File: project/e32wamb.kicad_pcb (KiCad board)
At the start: 2 copper layers, 50 x 37 mm, 34 parts, among them J1 2059-302_998-403, J2 Conn_01x04, J3 Conn_01x03, Q1 AO3400, Q2 AO3400, Q3 AO3400, Q4 AO3400, Q5 AO3400, SW1 TS-1187A-B-A-B, U1 AP63203WU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

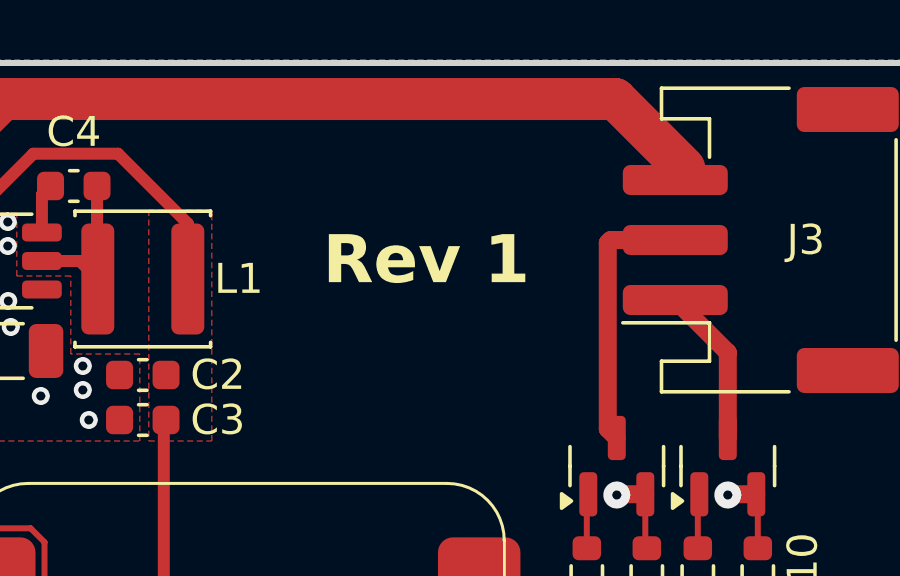
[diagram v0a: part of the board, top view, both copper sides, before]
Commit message: Add rotation offset for U1 (for jlcfab), bump revision
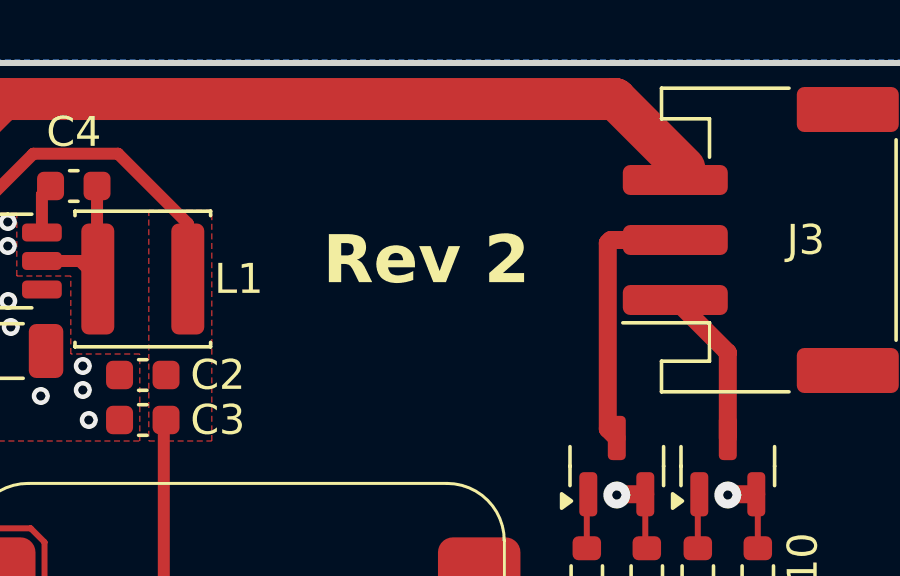
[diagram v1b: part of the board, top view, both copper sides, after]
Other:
- board text added: "Rev 2"
- board text removed: "Rev 1"
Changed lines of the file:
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@@
 	(title_block
 		(title "e32wamb pcb")
-		(date "2025-04-08")
-		(rev "1")
+		(date "2025-04-09")
+		(rev "2")
 		(company "wejn.org")
 		(comment 1 "Licensed under CC BY-SA 4.0")
@@
 			)
 		)
+		(property "FT Rotation Offset" "90"
+			(at 0 0 0)
+			(unlocked yes)
+			(layer "F.Fab")
+			(hide yes)
+			(effects
+				(font
+					(size 1 1)
+					(thickness 0.15)
+				)
+			)
+		)
 		(property ki_fp_filters "TSOT?23*")
 		(sheetname "/")
@@
 		)
 	)
-	(gr_text "Rev 1"
+	(gr_text "Rev 2"
 		(at 80.1 57.5 0)
 		(layer "F.SilkS")

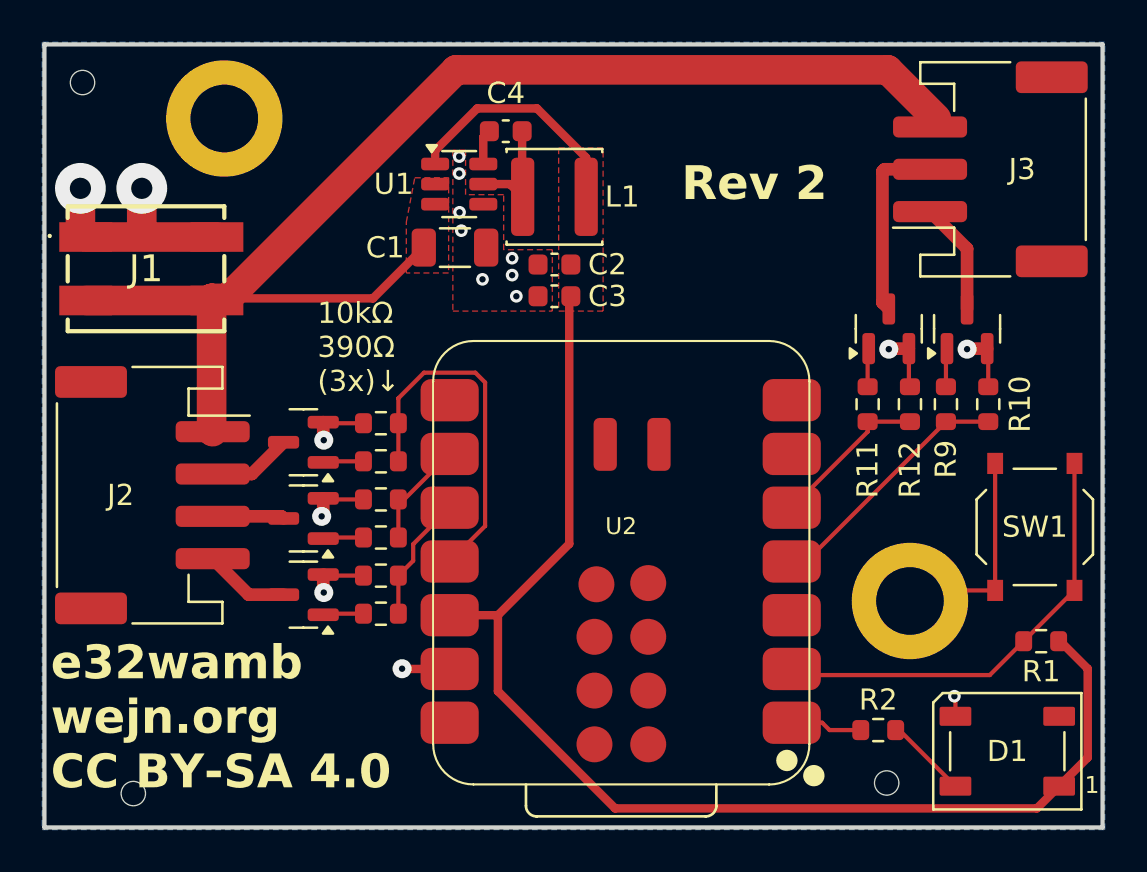
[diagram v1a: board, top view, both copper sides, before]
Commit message: Tune spacing between mounting holes; switch to vars for revision + date
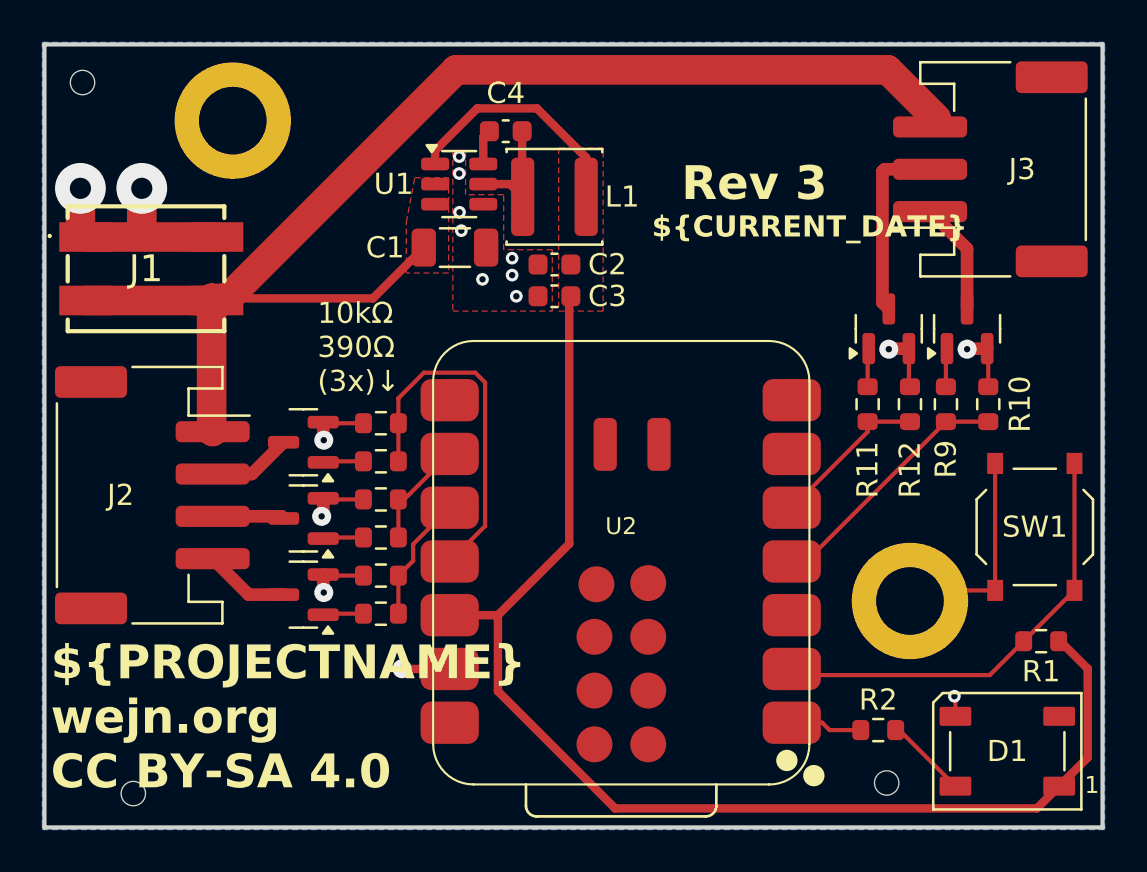
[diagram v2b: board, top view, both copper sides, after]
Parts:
- moved H1 0.41 mm to (58.9, 53.6)
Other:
- board text added: "${CURRENT_DATE}"
- board text added: "${PROJECTNAME} ${COMPANY} CC BY-SA 4.0"
- board text added: "Rev ${REVISION}"
- board text removed: "Rev 2"
- board text removed: "e32wamb wejn.org CC BY-SA 4.0"
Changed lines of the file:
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@@
 	(title_block
 		(title "e32wamb pcb")
-		(date "2025-04-09")
-		(rev "2")
+		(date "${CURRENT_DATE}")
+		(rev "3")
 		(company "wejn.org")
 		(comment 1 "Licensed under CC BY-SA 4.0")
@@
 	(footprint "MountingHole:MountingHole_3.2mm_M3_ISO14580_Pad"
 		(layer "F.Cu")
-		(at 58.5 53.5)
+		(at 58.9 53.6)
 		(descr "Mounting Hole 3.2mm, M3, ISO14580")
 		(tags "mounting hole 3.2mm m3 iso14580")
@@
 		(layer "Edge.Cuts")
 	)
+	(gr_text "${CURRENT_DATE}"
+		(at 78.7 59.2 0)
+		(layer "F.SilkS")
+		(effects
+			(font
+				(size 1 1)
+				(thickness 0.2)
+				(bold yes)
+			)
+			(justify left bottom)
+		)
+	)
 	(gr_text "10kΩ\n390Ω\n(3x)↓"
 		(at 62.9 66.5 0)
@@
 		)
 	)
-	(gr_text "e32wamb\nwejn.org\nCC BY-SA 4.0"
+	(gr_text "${PROJECTNAME}\n${COMPANY}\nCC BY-SA 4.0"
 		(at 50.3 85.3 0)
 		(layer "F.SilkS")
@@
 		)
 	)
-	(gr_text "Rev 2"
+	(gr_text "Rev ${REVISION}"
 		(at 80.1 57.5 0)
 		(layer "F.SilkS")

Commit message: Add keepout zone around the antenna
I thought I could do without because I'll be using an external antenna,
but it hardly costs anything. So why not have the keepout just in case.
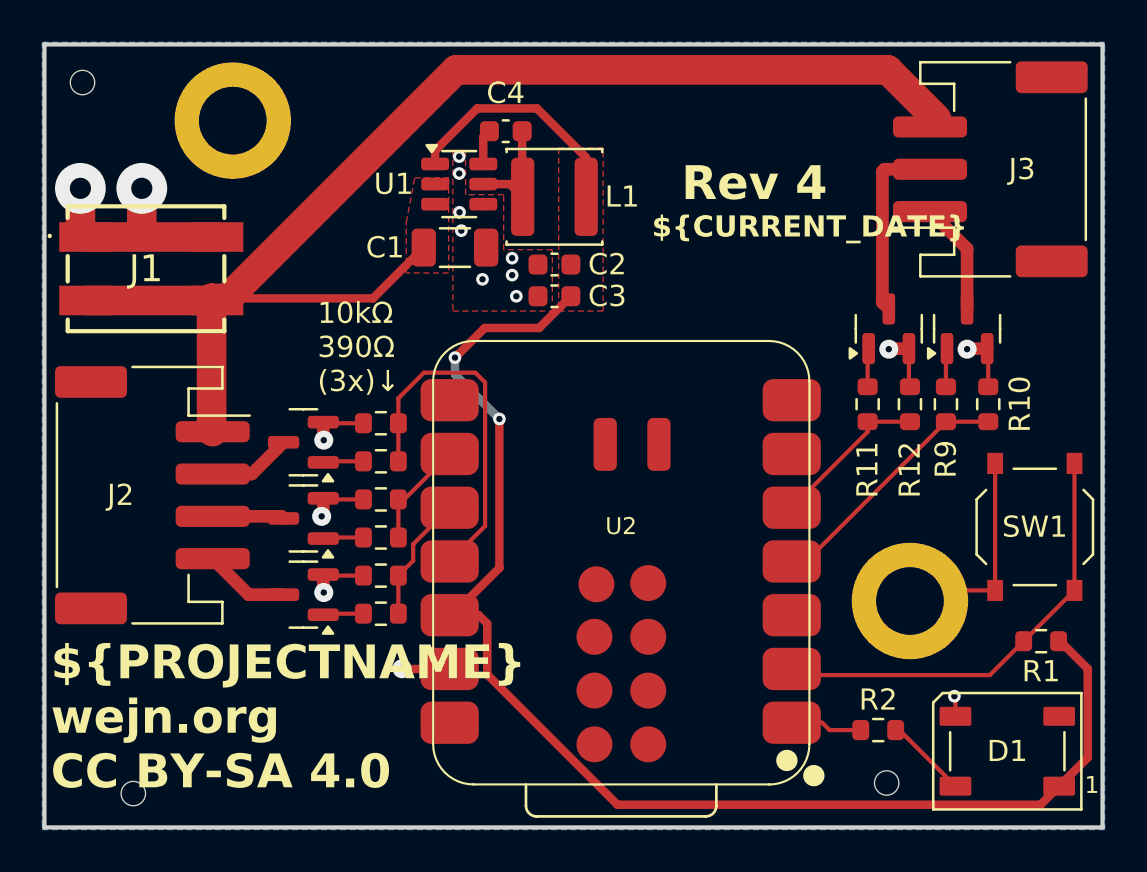
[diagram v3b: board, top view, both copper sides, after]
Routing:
- net +3.3V: track 70.7 -> 74.1 mm, vias 0 -> 2
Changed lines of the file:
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@@
 		(title "e32wamb pcb")
 		(date "${CURRENT_DATE}")
-		(rev "3")
+		(rev "4")
 		(company "wejn.org")
 		(comment 1 "Licensed under CC BY-SA 4.0")
@@
 	)
 	(segment
-		(start 71.4283 76.9717)
-		(end 69.1486 76.9717)
-		(width 0.4)
-		(layer "F.Cu")
-		(net 3)
-	)
-	(segment
 		(start 99.3 79.5)
 		(end 99.3 83.7)
@@
 	)
 	(segment
-		(start 71.4283 80.561524)
-		(end 71.4283 76.9717)
+		(start 97.073 85.927)
+		(end 77.076618 85.927)
 		(width 0.4)
 		(layer "F.Cu")
@@
 	)
 	(segment
-		(start 76.967776 86.101)
-		(end 71.4283 80.561524)
+		(start 74.875 61.9)
+		(end 73.376 63.399)
 		(width 0.4)
 		(layer "F.Cu")
@@
 	)
 	(segment
-		(start 96.899 86.101)
-		(end 76.967776 86.101)
+		(start 70.451626 53.024)
+		(end 68.4625 55.013126)
 		(width 0.4)
 		(layer "F.Cu")
@@
 	)
 	(segment
-		(start 74.8 61.9)
-		(end 74.8 73.6)
+		(start 97.925 78.2)
+		(end 98 78.2)
 		(width 0.4)
 		(layer "F.Cu")
@@
 	)
 	(segment
-		(start 70.451626 53.024)
-		(end 68.4625 55.013126)
+		(start 97.95 85.05)
+		(end 97.073 85.927)
 		(width 0.4)
 		(layer "F.Cu")
@@
 	)
 	(segment
-		(start 74.8 73.6)
-		(end 71.4283 76.9717)
+		(start 71.5 74.736778)
+		(end 69.265078 76.9717)
 		(width 0.4)
 		(layer "F.Cu")
@@
 	)
 	(segment
-		(start 97.925 78.2)
-		(end 98 78.2)
+		(start 73.274 53.024)
+		(end 70.451626 53.024)
 		(width 0.4)
 		(layer "F.Cu")
@@
 	)
 	(segment
-		(start 73.274 53.024)
-		(end 70.451626 53.024)
+		(start 70.9246 79.774982)
+		(end 70.9246 77.3727)
 		(width 0.4)
 		(layer "F.Cu")
@@
 	)
 	(segment
-		(start 97.95 85.05)
-		(end 96.899 86.101)
+		(start 70.5236 76.9717)
+		(end 69.1486 76.9717)
+		(width 0.4)
+		(layer "F.Cu")
+		(net 3)
+	)
+	(segment
+		(start 70.801 63.399)
+		(end 69.4 64.8)
+		(width 0.4)
+		(layer "F.Cu")
+		(net 3)
+	)
+	(segment
+		(start 71.5 67.7)
+		(end 71.5 74.736778)
+		(width 0.4)
+		(layer "F.Cu")
+		(net 3)
+	)
+	(segment
+		(start 70.9246 77.3727)
+		(end 70.5236 76.9717)
+		(width 0.4)
+		(layer "F.Cu")
+		(net 3)
+	)
+	(segment
+		(start 77.076618 85.927)
+		(end 70.9246 79.774982)
 		(width 0.4)
 		(layer "F.Cu")
@@
 	)
 	(segment
+		(start 73.376 63.399)
+		(end 70.801 63.399)
+		(width 0.4)
+		(layer "F.Cu")
+		(net 3)
+	)
+	(via
+		(at 71.5 67.7)
+		(size 0.6)
+		(drill 0.3)
+		(layers "F.Cu" "B.Cu")
+		(net 3)
+	)
+	(via
+		(at 69.4 64.8)
+		(size 0.6)
+		(drill 0.3)
+		(layers "F.Cu" "B.Cu")
+		(net 3)
+	)
+	(segment
+		(start 71.5 67.7)
+		(end 69.4 65.6)
+		(width 0.4)
+		(layer "B.Cu")
+		(net 3)
+	)
+	(segment
+		(start 69.4 65.6)
+		(end 69.4 64.8)
+		(width 0.4)
+		(layer "B.Cu")
+		(net 3)
+	)
+	(segment
 		(start 70.7375 56.6)
 		(end 72 56.6)
@@
 			)
 		)
+	)
+	(zone
+		(net 0)
+		(net_name "")
+		(layers "F.Cu" "B.Cu")
+		(hatch edge 0.5)
+		(connect_pads
+			(clearance 0)
+		)
+		(min_thickness 0.25)
+		(filled_areas_thickness no)
+		(keepout
+			(tracks not_allowed)
+			(vias not_allowed)
+			(pads not_allowed)
+			(copperpour not_allowed)
+			(footprints allowed)
+		)
+		(placement
+			(enabled no)
+			(sheetname "")
+		)
+		(fill
+			(thermal_gap 0.5)
+			(thermal_bridge_width 0.5)
+		)
+		(polygon
+			(pts
+				(xy 83.3 63.6) (xy 83.3 66.7) (xy 71.2 66.7) (xy 71.2 63.6)
+			)
+		)
